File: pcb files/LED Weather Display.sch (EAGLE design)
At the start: 8 parts, among them IC1 74HCT245N, J1 POWER_JACK

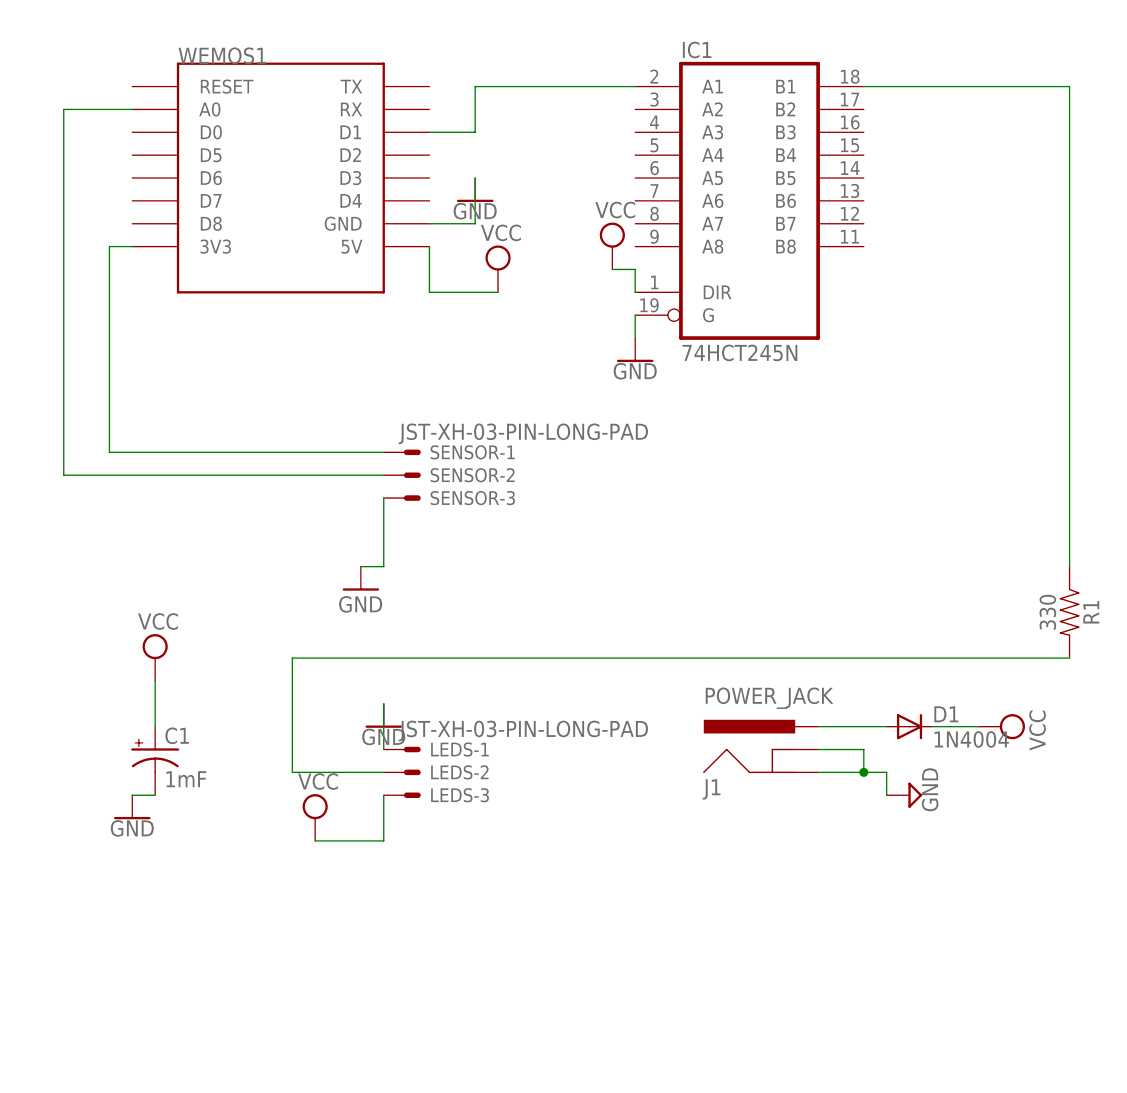
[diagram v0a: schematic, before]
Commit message: Update for digital light sensor.
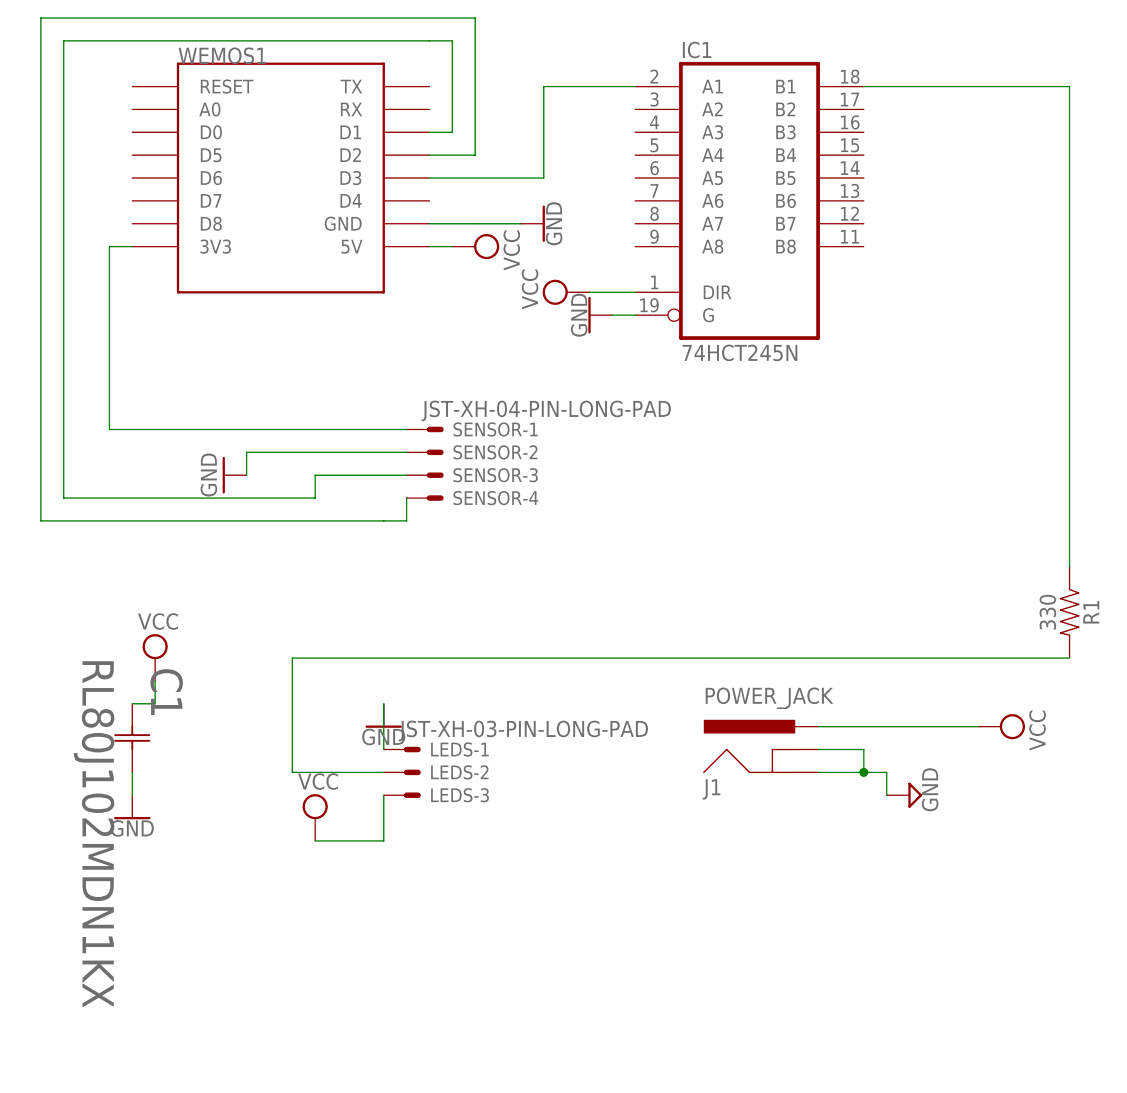
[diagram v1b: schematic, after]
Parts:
- removed D1: 1N4004, diode:1N4004
- C1: value 1mF -> RL80J102MDN1KX; device SparkFun-Capacitors:1000UF-RADIAL-5MM-25V-20% -> Kyle's Custom:RL80J102MDN1KX
- SENSOR: value JST-XH-03-PIN-LONG-PAD -> JST-XH-04-PIN-LONG-PAD; device Rembrandt Electronics - JST XH Connectors v1-0:JST-XH-03-PIN-LONG-PAD -> Rembrandt Electronics - JST XH Connectors v1-0:JST-XH-04-PIN-LONG-PAD
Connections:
- removed net N$1 (its old number): SENSOR-2.S, WEMOS1.A0
- new net N$5: SENSOR-3.S, WEMOS1.D1
- net GND: now also C1.22, SENSOR-2.S; no longer C1.-, SENSOR-3.S
- net N$3: now also WEMOS1.D3; no longer WEMOS1.D1
- net N$6: now also SENSOR-4.S, WEMOS1.D2; no longer D1.A, J1.PWR
- net VCC: now also C1.11, J1.PWR; no longer C1.+, D1.C
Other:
- moved on the sheet: SENSOR-1, SENSOR-2, SENSOR-3
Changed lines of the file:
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@@
 <part name="WEMOS1" library="esp8266modules" deviceset="WEMOS-D1-MINI" device=""/>
 <part name="LEDS" library="Rembrandt Electronics - JST XH Connectors v1-0" deviceset="JST-XH-03-PIN" device="-LONG-PAD"/>
-<part name="C1" library="SparkFun-Capacitors" library_urn="urn:adsk.eagle:library:510" deviceset="1000UF" device="-RADIAL-5MM-25V-20%" package3d_urn="urn:adsk.eagle:package:37412/1" value="1mF"/>
 <part name="R1" library="SparkFun-Resistors" library_urn="urn:adsk.eagle:library:532" deviceset="330OHM" device="-HORIZ-1/10W-5%" package3d_urn="urn:adsk.eagle:package:39658/1" value="330"/>
 <part name="IC1" library="74xx-eu" library_urn="urn:adsk.eagle:library:85" deviceset="74*245" device="N" package3d_urn="urn:adsk.eagle:package:2017/1" technology="HCT"/>
@@
 <part name="GND3" library="SparkFun-PowerSymbols" library_urn="urn:adsk.eagle:library:530" deviceset="GND" device=""/>
 <part name="GND4" library="SparkFun-PowerSymbols" library_urn="urn:adsk.eagle:library:530" deviceset="GND" device=""/>
-<part name="SENSOR" library="Rembrandt Electronics - JST XH Connectors v1-0" deviceset="JST-XH-03-PIN" device="-LONG-PAD"/>
 <part name="GND5" library="supply1" library_urn="urn:adsk.eagle:library:371" deviceset="GND" device=""/>
-<part name="D1" library="diode" library_urn="urn:adsk.eagle:library:210" deviceset="1N4004" device="" package3d_urn="urn:adsk.eagle:package:43336/1"/>
+<part name="C1" library="Kyle's Custom" deviceset="RL80J102MDN1KX" device=""/>
+<part name="SENSOR" library="Rembrandt Electronics - JST XH Connectors v1-0" deviceset="JST-XH-04-PIN" device="-LONG-PAD"/>
 </parts>
 <sheets>
@@
 <instance part="LEDS" gate="-2" x="30.48" y="2.54"/>
 <instance part="LEDS" gate="-3" x="30.48" y="0"/>
-<instance part="C1" gate="G$1" x="2.54" y="5.08"/>
 <instance part="R1" gate="G$1" x="104.14" y="20.32" rot="R270"/>
 <instance part="IC1" gate="A" x="68.58" y="66.04"/>
@@
 <instance part="SUPPLY2" gate="GND" x="86.36" y="0" rot="R90"/>
 <instance part="J1" gate="G$1" x="73.66" y="0"/>
-<instance part="SUPPLY3" gate="G$1" x="53.34" y="60.96"/>
-<instance part="SUPPLY4" gate="G$1" x="40.64" y="58.42"/>
+<instance part="SUPPLY3" gate="G$1" x="48.26" y="55.88" rot="R90"/>
+<instance part="SUPPLY4" gate="G$1" x="38.1" y="60.96" rot="R270"/>
 <instance part="SUPPLY5" gate="G$1" x="20.32" y="-2.54"/>
 <instance part="SUPPLY6" gate="G$1" x="2.54" y="15.24"/>
 <instance part="GND1" gate="1" x="0" y="-2.54"/>
 <instance part="GND2" gate="1" x="27.94" y="7.62"/>
-<instance part="GND3" gate="1" x="38.1" y="66.04"/>
-<instance part="GND4" gate="1" x="55.88" y="48.26"/>
-<instance part="SENSOR" gate="-1" x="30.48" y="38.1"/>
-<instance part="SENSOR" gate="-2" x="30.48" y="35.56"/>
-<instance part="SENSOR" gate="-3" x="30.48" y="33.02"/>
-<instance part="GND5" gate="1" x="25.4" y="22.86"/>
-<instance part="D1" gate="1" x="86.36" y="7.62"/>
+<instance part="GND3" gate="1" x="45.72" y="63.5" rot="R90"/>
+<instance part="GND4" gate="1" x="50.8" y="53.34" rot="R270"/>
+<instance part="GND5" gate="1" x="10.16" y="35.56" rot="R270"/>
+<instance part="C1" gate="A" x="0" y="10.16" rot="R270"/>
+<instance part="SENSOR" gate="-1" x="33.02" y="40.64"/>
+<instance part="SENSOR" gate="-2" x="33.02" y="38.1"/>
+<instance part="SENSOR" gate="-3" x="33.02" y="35.56"/>
+<instance part="SENSOR" gate="-4" x="33.02" y="33.02"/>
 </instances>
 <busses>
@@
 <net name="N$3" class="0">
 <segment>
-<pinref part="WEMOS1" gate="D1" pin="D1"/>
-<wire x1="33.02" y1="73.66" x2="38.1" y2="73.66" width="0.1524" layer="91"/>
-<wire x1="38.1" y1="73.66" x2="38.1" y2="78.74" width="0.1524" layer="91"/>
 <pinref part="IC1" gate="A" pin="A1"/>
-<wire x1="38.1" y1="78.74" x2="55.88" y2="78.74" width="0.1524" layer="91"/>
+<wire x1="45.72" y1="78.74" x2="55.88" y2="78.74" width="0.1524" layer="91"/>
+<pinref part="WEMOS1" gate="D1" pin="D3"/>
+<wire x1="33.02" y1="68.58" x2="45.72" y2="68.58" width="0.1524" layer="91"/>
+<wire x1="45.72" y1="68.58" x2="45.72" y2="78.74" width="0.1524" layer="91"/>
 </segment>
 </net>
@@
 <net name="VCC" class="0">
 <segment>
-<pinref part="SUPPLY4" gate="G$1" pin="VCC"/>
-<pinref part="WEMOS1" gate="D1" pin="5V"/>
-<wire x1="40.64" y1="55.88" x2="33.02" y2="55.88" width="0.1524" layer="91"/>
-<wire x1="33.02" y1="55.88" x2="33.02" y2="60.96" width="0.1524" layer="91"/>
-</segment>
-<segment>
-<pinref part="SUPPLY3" gate="G$1" pin="VCC"/>
-<pinref part="IC1" gate="A" pin="DIR"/>
-<wire x1="53.34" y1="58.42" x2="55.88" y2="58.42" width="0.1524" layer="91"/>
-<wire x1="55.88" y1="58.42" x2="55.88" y2="55.88" width="0.1524" layer="91"/>
-</segment>
-<segment>
-<pinref part="SUPPLY6" gate="G$1" pin="VCC"/>
-<pinref part="C1" gate="G$1" pin="+"/>
-<wire x1="2.54" y1="12.7" x2="2.54" y2="7.62" width="0.1524" layer="91"/>
-</segment>
-<segment>
 <pinref part="SUPPLY5" gate="G$1" pin="VCC"/>
 <pinref part="LEDS" gate="-3" pin="S"/>
@@
 </segment>
 <segment>
-<pinref part="D1" gate="1" pin="C"/>
 <pinref part="SUPPLY1" gate="G$1" pin="VCC"/>
-<wire x1="88.9" y1="7.62" x2="93.98" y2="7.62" width="0.1524" layer="91"/>
+<pinref part="J1" gate="G$1" pin="PWR"/>
+<wire x1="93.98" y1="7.62" x2="76.2" y2="7.62" width="0.1524" layer="91"/>
+</segment>
+<segment>
+<pinref part="C1" gate="A" pin="11"/>
+<pinref part="SUPPLY6" gate="G$1" pin="VCC"/>
+<wire x1="0" y1="10.16" x2="2.54" y2="10.16" width="0.1524" layer="91"/>
+<wire x1="2.54" y1="10.16" x2="2.54" y2="12.7" width="0.1524" layer="91"/>
+</segment>
+<segment>
+<pinref part="WEMOS1" gate="D1" pin="5V"/>
+<pinref part="SUPPLY4" gate="G$1" pin="VCC"/>
+<wire x1="33.02" y1="60.96" x2="35.56" y2="60.96" width="0.1524" layer="91"/>
+</segment>
+<segment>
+<pinref part="SUPPLY3" gate="G$1" pin="VCC"/>
+<pinref part="IC1" gate="A" pin="DIR"/>
+<wire x1="50.8" y1="55.88" x2="55.88" y2="55.88" width="0.1524" layer="91"/>
 </segment>
 </net>
@@
 <pinref part="GND3" gate="1" pin="GND"/>
 <pinref part="WEMOS1" gate="D1" pin="GND"/>
-<wire x1="38.1" y1="68.58" x2="38.1" y2="63.5" width="0.1524" layer="91"/>
+<wire x1="43.18" y1="63.5" x2="38.1" y2="63.5" width="0.1524" layer="91"/>
 <wire x1="38.1" y1="63.5" x2="33.02" y2="63.5" width="0.1524" layer="91"/>
 </segment>
@@
 <pinref part="GND4" gate="1" pin="GND"/>
 <pinref part="IC1" gate="A" pin="G"/>
-<wire x1="55.88" y1="50.8" x2="55.88" y2="53.34" width="0.1524" layer="91"/>
-</segment>
-<segment>
-<pinref part="GND1" gate="1" pin="GND"/>
-<pinref part="C1" gate="G$1" pin="-"/>
-<wire x1="0" y1="0" x2="2.54" y2="0" width="0.1524" layer="91"/>
+<wire x1="53.34" y1="53.34" x2="55.88" y2="53.34" width="0.1524" layer="91"/>
 </segment>
 <segment>
@@
 </segment>
 <segment>
-<pinref part="SENSOR" gate="-3" pin="S"/>
+<pinref part="GND1" gate="1" pin="GND"/>
+<pinref part="C1" gate="A" pin="22"/>
+<wire x1="0" y1="0" x2="0" y2="2.54" width="0.1524" layer="91"/>
+</segment>
+<segment>
 <pinref part="GND5" gate="1" pin="GND"/>
-<wire x1="27.94" y1="33.02" x2="27.94" y2="25.4" width="0.1524" layer="91"/>
-<wire x1="27.94" y1="25.4" x2="25.4" y2="25.4" width="0.1524" layer="91"/>
+<pinref part="SENSOR" gate="-2" pin="S"/>
+<wire x1="12.7" y1="35.56" x2="12.7" y2="38.1" width="0.1524" layer="91"/>
+<wire x1="12.7" y1="38.1" x2="30.48" y2="38.1" width="0.1524" layer="91"/>
 </segment>
 </net>
 <net name="N$1" class="0">
 <segment>
-<pinref part="WEMOS1" gate="D1" pin="A0"/>
-<wire x1="0" y1="76.2" x2="-7.62" y2="76.2" width="0.1524" layer="91"/>
-<pinref part="SENSOR" gate="-2" pin="S"/>
-<wire x1="-7.62" y1="76.2" x2="-7.62" y2="35.56" width="0.1524" layer="91"/>
-<wire x1="-7.62" y1="35.56" x2="27.94" y2="35.56" width="0.1524" layer="91"/>
+<pinref part="WEMOS1" gate="D1" pin="3V3"/>
+<wire x1="-2.54" y1="60.96" x2="0" y2="60.96" width="0.1524" layer="91"/>
+<pinref part="SENSOR" gate="-1" pin="S"/>
+<wire x1="-2.54" y1="60.96" x2="-2.54" y2="40.64" width="0.1524" layer="91"/>
+<wire x1="-2.54" y1="40.64" x2="30.48" y2="40.64" width="0.1524" layer="91"/>
 </segment>
 </net>
 <net name="N$5" class="0">
 <segment>
-<pinref part="SENSOR" gate="-1" pin="S"/>
-<wire x1="27.94" y1="38.1" x2="-2.54" y2="38.1" width="0.1524" layer="91"/>
-<pinref part="WEMOS1" gate="D1" pin="3V3"/>
-<wire x1="-2.54" y1="38.1" x2="-2.54" y2="60.96" width="0.1524" layer="91"/>
-<wire x1="-2.54" y1="60.96" x2="0" y2="60.96" width="0.1524" layer="91"/>
+<pinref part="WEMOS1" gate="D1" pin="D1"/>
+<wire x1="33.02" y1="73.66" x2="35.56" y2="73.66" width="0.1524" layer="91"/>
+<wire x1="35.56" y1="73.66" x2="35.56" y2="83.82" width="0.1524" layer="91"/>
+<wire x1="35.56" y1="83.82" x2="33.02" y2="83.82" width="0.1524" layer="91"/>
+<wire x1="33.02" y1="83.82" x2="-7.62" y2="83.82" width="0.1524" layer="91"/>
+<wire x1="-7.62" y1="83.82" x2="-7.62" y2="33.02" width="0.1524" layer="91"/>
+<wire x1="-7.62" y1="33.02" x2="20.32" y2="33.02" width="0.1524" layer="91"/>
+<wire x1="20.32" y1="33.02" x2="20.32" y2="35.56" width="0.1524" layer="91"/>
+<pinref part="SENSOR" gate="-3" pin="S"/>
+<wire x1="20.32" y1="35.56" x2="30.48" y2="35.56" width="0.1524" layer="91"/>
 </segment>
 </net>
 <net name="N$6" class="0">
 <segment>
-<pinref part="J1" gate="G$1" pin="PWR"/>
-<pinref part="D1" gate="1" pin="A"/>
-<wire x1="76.2" y1="7.62" x2="83.82" y2="7.62" width="0.1524" layer="91"/>
+<pinref part="WEMOS1" gate="D1" pin="D2"/>
+<wire x1="33.02" y1="71.12" x2="38.1" y2="71.12" width="0.1524" layer="91"/>
+<wire x1="38.1" y1="71.12" x2="38.1" y2="86.36" width="0.1524" layer="91"/>
+<wire x1="38.1" y1="86.36" x2="-10.16" y2="86.36" width="0.1524" layer="91"/>
+<wire x1="-10.16" y1="86.36" x2="-10.16" y2="30.48" width="0.1524" layer="91"/>
+<wire x1="-10.16" y1="30.48" x2="27.94" y2="30.48" width="0.1524" layer="91"/>
+<pinref part="SENSOR" gate="-4" pin="S"/>
+<wire x1="27.94" y1="30.48" x2="30.48" y2="30.48" width="0.1524" layer="91"/>
+<wire x1="30.48" y1="30.48" x2="30.48" y2="33.02" width="0.1524" layer="91"/>
 </segment>
 </net>

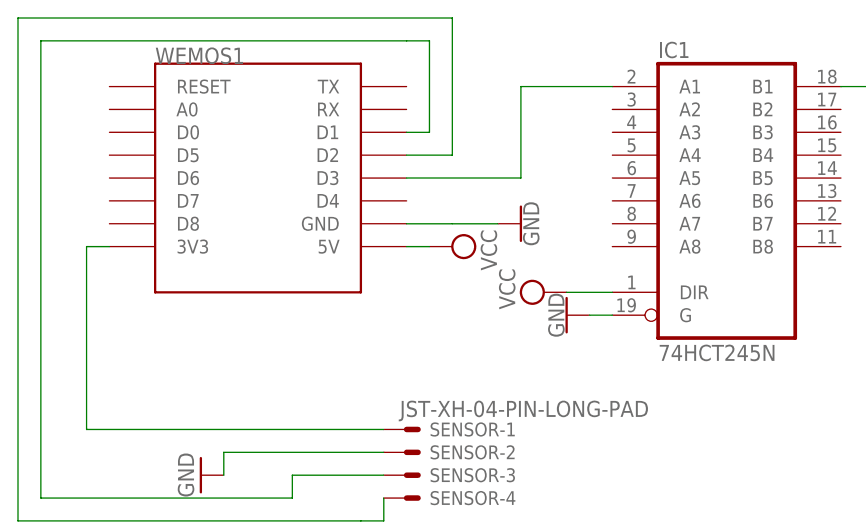
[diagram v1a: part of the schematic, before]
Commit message: Update board layouts and kit information in documentation.
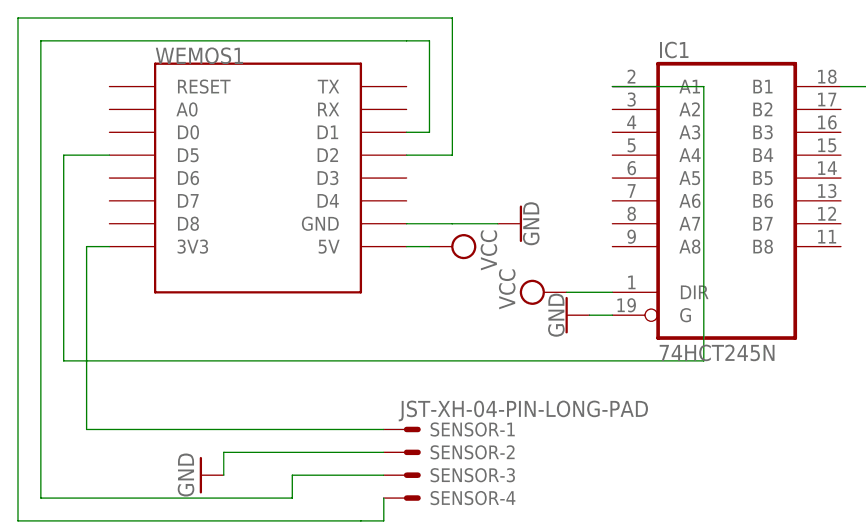
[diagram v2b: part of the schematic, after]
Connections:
- net N$3: now also WEMOS1.D5; no longer WEMOS1.D3
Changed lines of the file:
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@@
-</segment>
-</net>
-<net name="N$3" class="0">
-<segment>
-<pinref part="IC1" gate="A" pin="A1"/>
-<wire x1="45.72" y1="78.74" x2="55.88" y2="78.74" width="0.1524" layer="91"/>
-<pinref part="WEMOS1" gate="D1" pin="D3"/>
-<wire x1="33.02" y1="68.58" x2="45.72" y2="68.58" width="0.1524" layer="91"/>
-<wire x1="45.72" y1="68.58" x2="45.72" y2="78.74" width="0.1524" layer="91"/>
 </segment>
 </net>
@@
 </segment>
 </net>
+<net name="N$3" class="0">
+<segment>
+<pinref part="WEMOS1" gate="D1" pin="D5"/>
+<wire x1="0" y1="71.12" x2="-5.08" y2="71.12" width="0.1524" layer="91"/>
+<wire x1="-5.08" y1="71.12" x2="-5.08" y2="48.26" width="0.1524" layer="91"/>
+<wire x1="-5.08" y1="48.26" x2="66.04" y2="48.26" width="0.1524" layer="91"/>
+<pinref part="IC1" gate="A" pin="A1"/>
+<wire x1="66.04" y1="48.26" x2="66.04" y2="78.74" width="0.1524" layer="91"/>
+<wire x1="66.04" y1="78.74" x2="55.88" y2="78.74" width="0.1524" layer="91"/>
+</segment>
+</net>

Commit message: Update PCB files and documentation.
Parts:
- added PROGRAM: MOMENTARY-SWITCH-SPST-PTH-6.0MM, SparkFun-Switches:MOMENTARY-SWITCH-SPST-PTH-6.0MM
- added RESET: JST-XH-02-PIN-LONG-PAD, Rembrandt Electronics - JST XH Connectors v1-0:JST-XH-02-PIN-LONG-PAD
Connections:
- new net N$7: PROGRAM.1, WEMOS1.RESET
- new net N$8: RESET-2.S, WEMOS1.D6
- net GND: now also PROGRAM.2, RESET-1.S
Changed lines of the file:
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@@
 <part name="C1" library="Kyle's Custom" deviceset="RL80J102MDN1KX" device=""/>
 <part name="SENSOR" library="Rembrandt Electronics - JST XH Connectors v1-0" deviceset="JST-XH-04-PIN" device="-LONG-PAD"/>
+<part name="PROGRAM" library="SparkFun-Switches" library_urn="urn:adsk.eagle:library:535" deviceset="MOMENTARY-SWITCH-SPST" device="-PTH-6.0MM" package3d_urn="urn:adsk.eagle:package:40163/1"/>
+<part name="GND6" library="supply1" library_urn="urn:adsk.eagle:library:371" deviceset="GND" device=""/>
+<part name="RESET" library="Rembrandt Electronics - JST XH Connectors v1-0" deviceset="JST-XH-02-PIN" device="-LONG-PAD"/>
+<part name="GND7" library="supply1" library_urn="urn:adsk.eagle:library:371" deviceset="GND" device=""/>
 </parts>
 <sheets>
@@
 <instance part="SENSOR" gate="-3" x="33.02" y="35.56"/>
 <instance part="SENSOR" gate="-4" x="33.02" y="33.02"/>
+<instance part="PROGRAM" gate="G$1" x="15.24" y="25.4"/>
+<instance part="GND6" gate="1" x="27.94" y="25.4" rot="R90"/>
+<instance part="RESET" gate="-2" x="20.32" y="50.8"/>
+<instance part="RESET" gate="-1" x="20.32" y="53.34"/>
+<instance part="GND7" gate="1" x="10.16" y="53.34" rot="R270"/>
 </instances>
 <busses>
@@
 <wire x1="12.7" y1="35.56" x2="12.7" y2="38.1" width="0.1524" layer="91"/>
 <wire x1="12.7" y1="38.1" x2="30.48" y2="38.1" width="0.1524" layer="91"/>
+</segment>
+<segment>
+<pinref part="PROGRAM" gate="G$1" pin="2"/>
+<pinref part="GND6" gate="1" pin="GND"/>
+<wire x1="20.32" y1="25.4" x2="25.4" y2="25.4" width="0.1524" layer="91"/>
+</segment>
+<segment>
+<pinref part="GND7" gate="1" pin="GND"/>
+<pinref part="RESET" gate="-1" pin="S"/>
+<wire x1="12.7" y1="53.34" x2="17.78" y2="53.34" width="0.1524" layer="91"/>
 </segment>
 </net>
@@
 </segment>
 </net>
+<net name="N$7" class="0">
+<segment>
+<pinref part="PROGRAM" gate="G$1" pin="1"/>
+<wire x1="10.16" y1="25.4" x2="-12.7" y2="25.4" width="0.1524" layer="91"/>
+<pinref part="WEMOS1" gate="D1" pin="RESET"/>
+<wire x1="-12.7" y1="25.4" x2="-12.7" y2="78.74" width="0.1524" layer="91"/>
+<wire x1="-12.7" y1="78.74" x2="0" y2="78.74" width="0.1524" layer="91"/>
+</segment>
+</net>
+<net name="N$8" class="0">
+<segment>
+<pinref part="RESET" gate="-2" pin="S"/>
+<wire x1="17.78" y1="50.8" x2="0" y2="50.8" width="0.1524" layer="91"/>
+<pinref part="WEMOS1" gate="D1" pin="D6"/>
+<wire x1="0" y1="50.8" x2="0" y2="68.58" width="0.1524" layer="91"/>
+</segment>
+</net>
